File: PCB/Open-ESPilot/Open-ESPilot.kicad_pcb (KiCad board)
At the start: 2 copper layers, 108 parts, among them J1 USB_C_Receptacle_USB2.0_16P, J10 UART1, J11 UART2, J12 I2C, J13 Micro SD Card Breakout, J14 LED out, J2 VOUT, J3 VIN, J4 GND, J5 PWM output, J6 RC in, J7 Vx, J8 GND, J9 UART0, M1 Clone "MP1584" module, M2 GY91, Q1 AO3401A, Q2 BC847, Q3 BC847, SW1 SW_Push, SW2 SW_Push, U1 ESP32-S3-WROOM-1-N8, U2 AMS1117-3.3, U3 AMS1117-3.3, U4 INA219AxD, U5 Micro_SD_Card

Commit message: Started routing. I have few things there. Fixed schematic.
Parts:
- C25, C7, C9, J13, JP12, JP16, JP17, JP25, JP26, JP27, JP28, M1, U3, U5: moved to B.Cu
- C5: footprint Capacitor_THT:CP_Radial_D10.0mm_P5.00mm_P7.50mm -> Capacitor_THT:CP_Radial_D10.0mm_P5.00mm
- TP1, TP2, TP3: footprint TestPoint:TestPoint_THTPad_D2.0mm_Drill1.0mm -> TestPoint:TestPoint_Pad_2.0x2.0mm
- moved U5 310.5 mm to (198.5, -77.0), turned to 90 degrees
- moved J13 309.5 mm to (215.2, -86.8), turned to 180 degrees
- moved JP28 307.9 mm to (198.9, -66.5), turned to 90 degrees
- moved JP27 307.2 mm to (202.5, -66.5), turned to 90 degrees
- moved JP26 306.6 mm to (206.0, -66.5), turned to 90 degrees
- moved C25 304.2 mm to (209.0, -75.3), turned to -90 degrees
- moved J12 230.1 mm to (154.3, -71.2)
- moved R15 225.2 mm to (145.1, -66.1)
- moved R16 225.2 mm to (145.1, -63.2)
- moved C21 217.0 mm to (150.4, -47.2)
- moved JP22 213.7 mm to (133.1, -52.9)
- moved JP23 213.7 mm to (133.1, -49.3)
- moved JP15 192.4 mm to (128.7, -52.9)
- moved JP20 183.4 mm to (133.1, -60.0)
- moved JP21 183.4 mm to (133.1, -56.4)
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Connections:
- C24 pad 2: GND -> Net-(BZ1--)
- J14 pad 1: /Peripheral/5V -> +5V
- J5 pad 1: /Peripheral/ServoOutput1 -> /Peripheral/ServoOutput8
- J5 pad 2: /Peripheral/ServoOutput2 -> /Peripheral/ServoOutput7
- J5 pad 3: /Peripheral/ServoOutput3 -> /Peripheral/ServoOutput6
- J5 pad 4: /Peripheral/ServoOutput4 -> /Peripheral/ServoOutput5
- J5 pad 5: /Peripheral/ServoOutput5 -> /Peripheral/ServoOutput4
- J5 pad 6: /Peripheral/ServoOutput6 -> /Peripheral/ServoOutput3
- J5 pad 7: /Peripheral/ServoOutput7 -> /Peripheral/ServoOutput2
- J5 pad 8: /Peripheral/ServoOutput8 -> /Peripheral/ServoOutput1
- J6 pad 2: /Peripheral/5V -> +5V
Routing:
- net +5V: track 0.00 -> 24.0 mm, vias 0 -> 1
- net GND: track 0.00 -> 17.5 mm, vias 0 -> 1
- net VOUT: track 0.00 -> 16.1 mm
- net /MCU/USB_D+: track 0.00 -> 13.1 mm
- net /MCU/EN: track 0.00 -> 12.9 mm
- net /MCU/USB_D-: track 0.00 -> 12.5 mm
- net +3V3: track 0.00 -> 11.2 mm, vias 0 -> 1
- net /Peripheral/RCin_Inv: track 0.00 -> 11.2 mm, vias 0 -> 2
- net /MCU/GPIO35: track 0.00 -> 10.6 mm
- net Net-(JP2-A): track 0.00 -> 10.1 mm
- net /MCU/GPIO36: track 0.00 -> 9.96 mm
- net /MCU/GPIO44: track 0.00 -> 9.76 mm, vias 0 -> 1
- net Net-(JP3-A): track 0.00 -> 9.19 mm
- net /MCU/GPIO37: track 0.00 -> 9.18 mm
- net /MCU/GPIO38: track 0.00 -> 8.63 mm
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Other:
- board outline added: 50.1 x 91.9 mm

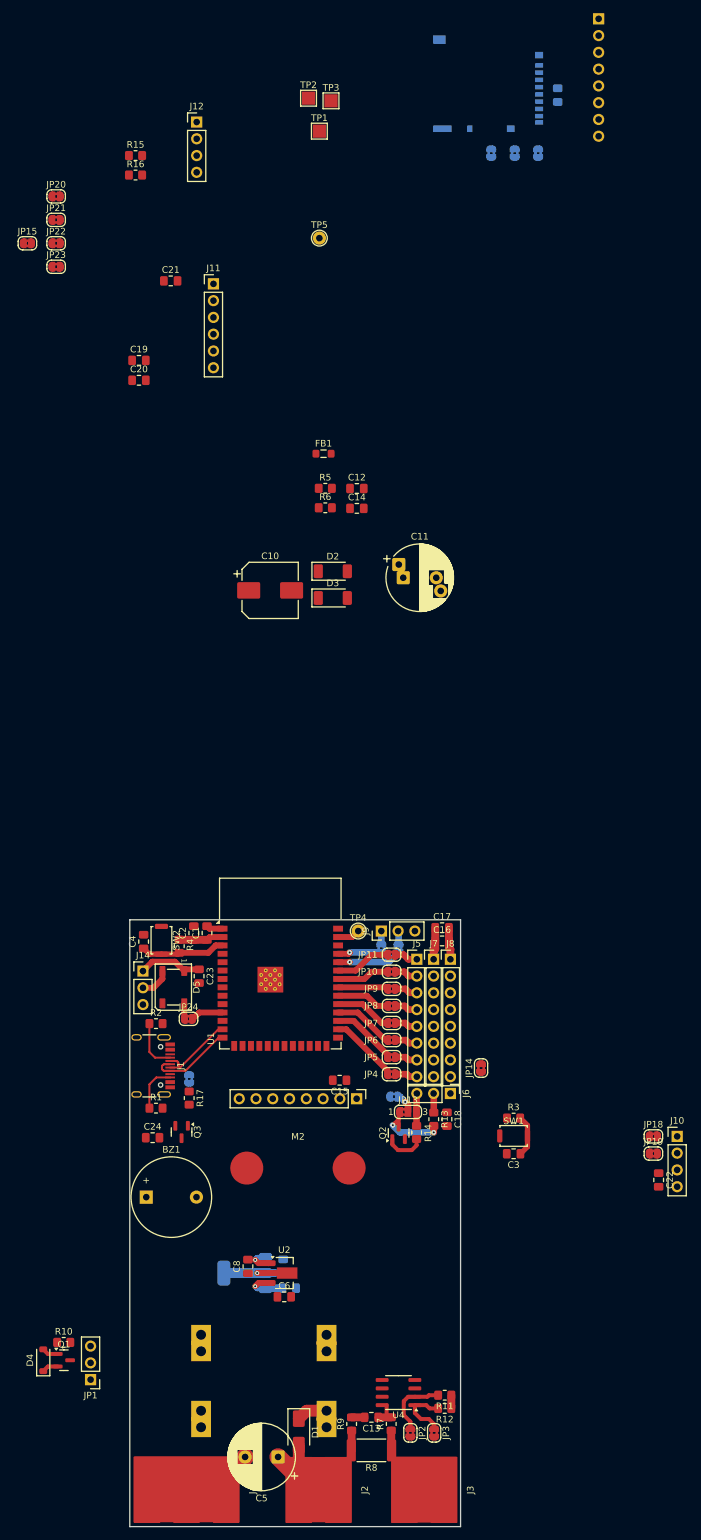
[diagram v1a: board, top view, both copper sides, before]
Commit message: halve of the PCB is routed.
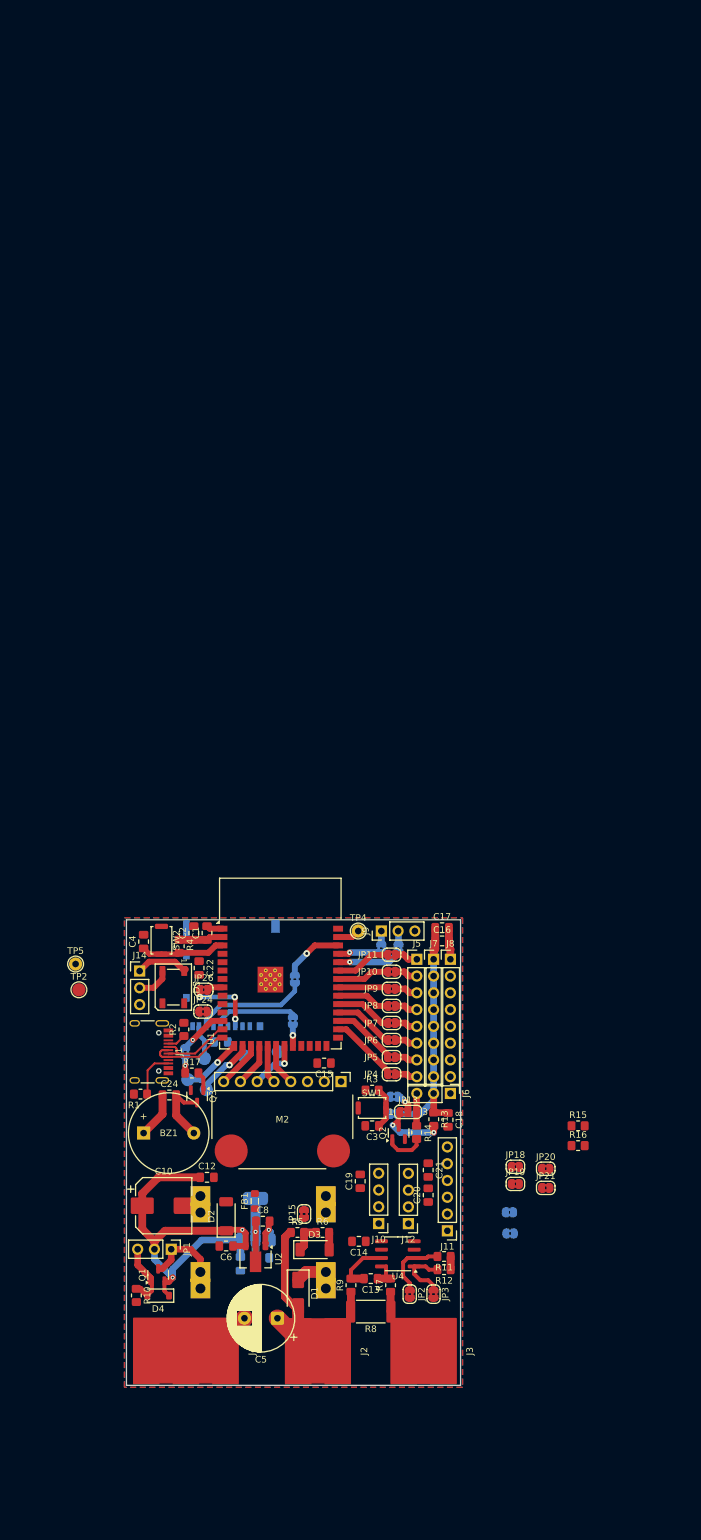
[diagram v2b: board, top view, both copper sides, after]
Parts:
- removed C11: 1000uF, Capacitor_THT:CP_Radial_D10.0mm_P5.00mm_P7.50mm
- removed the C19 at (145.6, -35.1)
- removed J13: Micro SD Card Breakout, Connector_PinHeader_2.54mm:PinHeader_1x08_P2.54mm_Vertical
- added TP6: SD-DAT1, TestPoint:TestPoint_Pad_D2.0mm, B.Cu at (155.5, 70.6)
- added TP7: SD-DAT2, TestPoint:TestPoint_Pad_D2.0mm, B.Cu at (166.7, 69.6)
- added TP8: SD-DAT3, TestPoint:TestPoint_Pad_D2.0mm, B.Cu at (161.5, 70.2)
- JP14: moved to B.Cu
- JP22: renamed from JP23; moved to B.Cu
- JP23: renamed from JP22; moved to B.Cu
- JP26: moved to F.Cu
- M2: footprint GY-90:GY-90 -> GY-91:GY-91
- TP1, TP3: footprint TestPoint:TestPoint_Pad_2.0x2.0mm -> TestPoint:TestPoint_Pad_D2.0mm; moved to B.Cu
- TP2: footprint TestPoint:TestPoint_Pad_2.0x2.0mm -> TestPoint:TestPoint_Pad_D2.0mm
- moved J12 169.9 mm to (186.4, 95.6), turned to 180 degrees
- moved JP23 165.0 mm to (201.8, 97.1), turned to 180 degrees
- moved JP20 164.9 mm to (207.2, 87.3)
- moved JP21 164.3 mm to (207.2, 90.2)
- moved R16 161.5 mm to (212.1, 83.8)
- moved R15 161.5 mm to (212.1, 80.8)
- moved JP22 158.8 mm to (201.7, 93.9), turned to 180 degrees
- moved JP15 152.9 mm to (170.6, 94.2), turned to 90 degrees
- moved C23 152.2 mm to (158.0, 68.1), turned to 180 degrees
- moved TP3 150.9 mm to (155.8, 75.3), turned to 180 degrees
- moved J11 147.7 mm to (192.3, 96.7), turned to 180 degrees
- moved TP1 145.0 mm to (153.0, 73.8), turned to 180 degrees
- moved U5 140.5 mm to (159.6, 58.0), turned to 0 degrees
- moved C21 140.2 mm to (189.4, 87.5), turned to -90 degrees
- moved TP2 139.4 mm to (136.5, 60.2)
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- renumbered C22 to C19, C23 to C22, C25 to C23
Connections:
- C16 pad 1: Net-(J7-Pin_1) -> /Peripheral/+5Vjp
- C17 pad 1: Net-(J7-Pin_1) -> /Peripheral/+5Vjp
- J10 pad 3: /Peripheral/5V -> +5V
- J11 pad 3: /Peripheral/5V -> +5V
- J12 pad 1: /Peripheral/SCL -> /Peripheral/SDA
- J12 pad 2: /Peripheral/SDA -> /Peripheral/SCL
- J12 pad 4: /Peripheral/5V -> +5V
- J6 pad 2: +5V -> /Peripheral/+5Vjp
- J7 pad 1: Net-(J7-Pin_1) -> /Peripheral/+5Vjp
- J7 pad 2: Net-(J7-Pin_1) -> /Peripheral/+5Vjp
- J7 pad 3: Net-(J7-Pin_1) -> /Peripheral/+5Vjp
- J7 pad 4: Net-(J7-Pin_1) -> /Peripheral/+5Vjp
- J7 pad 5: Net-(J7-Pin_1) -> /Peripheral/+5Vjp
- J7 pad 6: Net-(J7-Pin_1) -> /Peripheral/+5Vjp
- J7 pad 7: Net-(J7-Pin_1) -> /Peripheral/+5Vjp
- J7 pad 8: Net-(J7-Pin_1) -> /Peripheral/+5Vjp
- JP14 pad 1: Net-(J7-Pin_1) -> /Peripheral/+5Vjp
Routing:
- net +5V: track 24.0 -> 86.6 mm, vias 1 -> 2
- net /Peripheral/+5Vjp: track 0.00 -> 32.5 mm
- net /Peripheral/SD-DAT0: track 0.00 -> 17.4 mm
- net /Peripheral/SD-CLK: track 0.00 -> 12.9 mm
- net VOUT: track 16.1 -> 28.9 mm
- net /Power/+5Vreg: track 0.00 -> 10.9 mm
- net /Peripheral/SD-CMD: track 0.00 -> 10.9 mm, vias 0 -> 3
- net Net-(BZ1--): track 0.00 -> 10.5 mm
- net /MCU/GPIO2: track 0.00 -> 9.25 mm, vias 0 -> 1
- net /MCU/GPIO46: track 0.00 -> 9.16 mm, vias 0 -> 1
- net /MCU/GPIO3: track 0.00 -> 9.13 mm, vias 0 -> 1
- net /MCU/GPIO13: track 0.00 -> 7.98 mm, vias 0 -> 1
- net /Power/+5Vusb: track 2.48 -> 10.4 mm
- net /MCU/GPIO8: track 0.00 -> 7.32 mm, vias 0 -> 1
- net /MCU/GPIO9: track 0.00 -> 7.11 mm
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- added copper zone on B.Cu, net GND
- added copper zone on F.Cu, net GND
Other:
- board size 50.1 x 91.9 mm -> 50.6 x 70.5 mm

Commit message: I'm rushing it! :( Finished the PCB
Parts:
- C15, JP18, JP19, JP20, JP21, TP2: moved to B.Cu
- JP12: moved to F.Cu
- TP5: footprint TestPoint:TestPoint_THTPad_D2.0mm_Drill1.0mm -> TestPoint:TestPoint_Pad_D2.0mm; moved to B.Cu
- moved R15 36.0 mm to (178.1, 92.6)
- moved TP2 35.7 mm to (171.8, 65.8), turned to 180 degrees
- moved R16 35.7 mm to (178.1, 94.6)
- moved TP5 34.2 mm to (170.0, 52.9), turned to 180 degrees
- moved JP23 27.6 mm to (177.3, 84.4), turned to 90 degrees
- moved JP22 23.5 mm to (179.0, 87.8), turned to 90 degrees
- moved R10 19.5 mm to (164.3, 102.7), turned to 90 degrees
- moved JP19 18.2 mm to (184.4, 89.6), turned to 90 degrees
- moved JP20 17.6 mm to (189.8, 85.0), turned to 90 degrees
- moved JP21 17.2 mm to (192.3, 81.6), turned to 90 degrees
- moved JP18 14.9 mm to (188.8, 92.5), turned to 90 degrees
- moved D4 13.4 mm to (161.7, 104.0), turned to -90 degrees
- moved C19 10.4 mm to (189.4, 87.5)
- moved C21 10.4 mm to (179.0, 87.2)
- moved Q1 10.1 mm to (158.6, 104.0), turned to 180 degrees
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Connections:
- J6 pad 2: /Peripheral/+5Vjp -> +5V
- R3 pad 1: /MCU/+3V3p -> +3V3
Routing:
- net +5V: track 86.6 -> 235.2 mm, vias 2 -> 1
- net +3V3: track 12.8 -> 79.5 mm, vias 1 -> 3
- net /MCU/+3V3p: track 6.74 -> 68.3 mm, vias 0 -> 4
- net GND: track 21.4 -> 79.9 mm, vias 1 -> 57
- net /MCU/GPIO4: track 0.00 -> 55.9 mm, vias 0 -> 2
- net /Power/+5Vusb: track 10.4 -> 65.8 mm, vias 0 -> 2
- net /MCU/GPIO6: track 0.00 -> 55.2 mm, vias 0 -> 1
- net /MCU/GPIO16: track 0.00 -> 50.4 mm, vias 0 -> 1
- net /MCU/GPIO7: track 0.00 -> 49.0 mm, vias 0 -> 1
- net /MCU/GPIO17: track 0.00 -> 48.5 mm, vias 0 -> 1
- net /Peripheral/SCL: track 0.00 -> 33.1 mm, vias 0 -> 1
- net /Peripheral/SDA: track 0.00 -> 29.6 mm
- net /MCU/GPIO48: track 0.00 -> 24.5 mm, vias 0 -> 1
- net /MCU/GPIO47: track 0.00 -> 20.1 mm, vias 0 -> 1
- net /MCU/GPIO21: track 0.00 -> 18.6 mm
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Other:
- board size 50.6 x 70.5 mm -> 50.6 x 71.1 mm

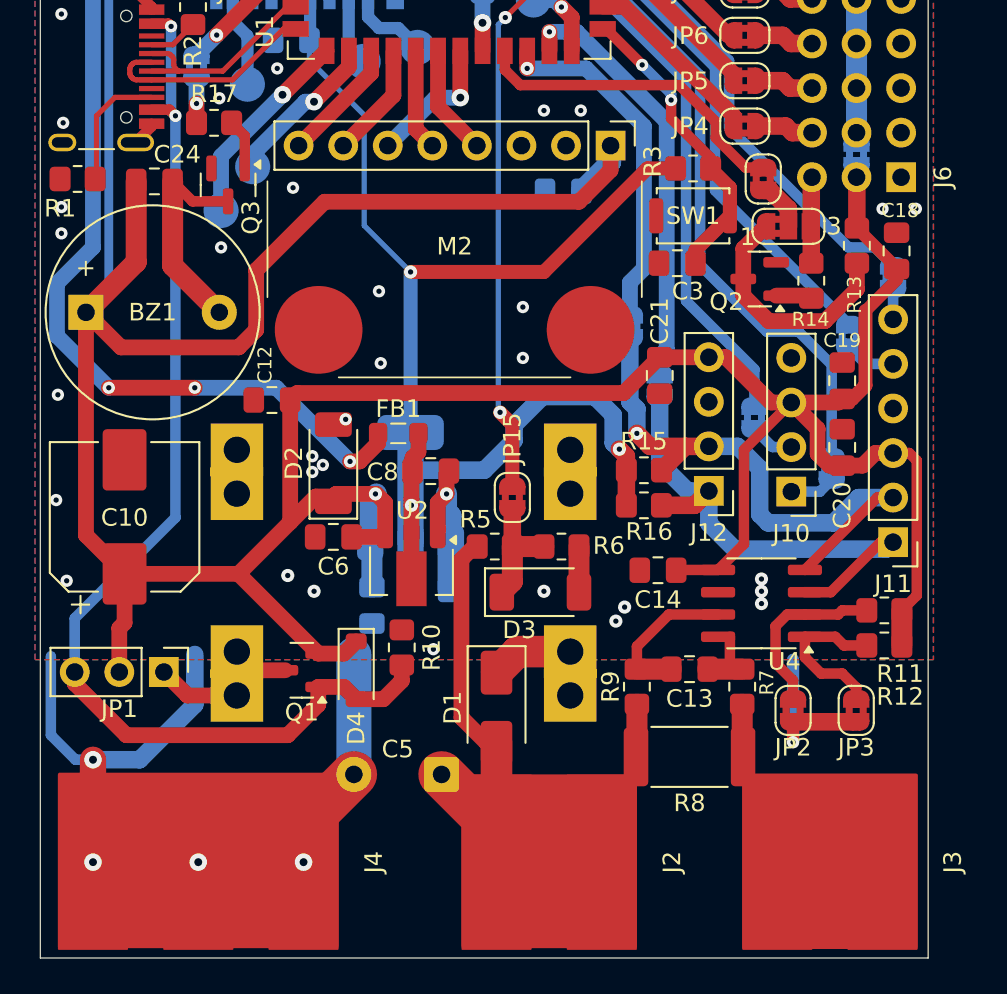
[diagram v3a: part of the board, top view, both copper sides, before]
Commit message: Added labels to headers.
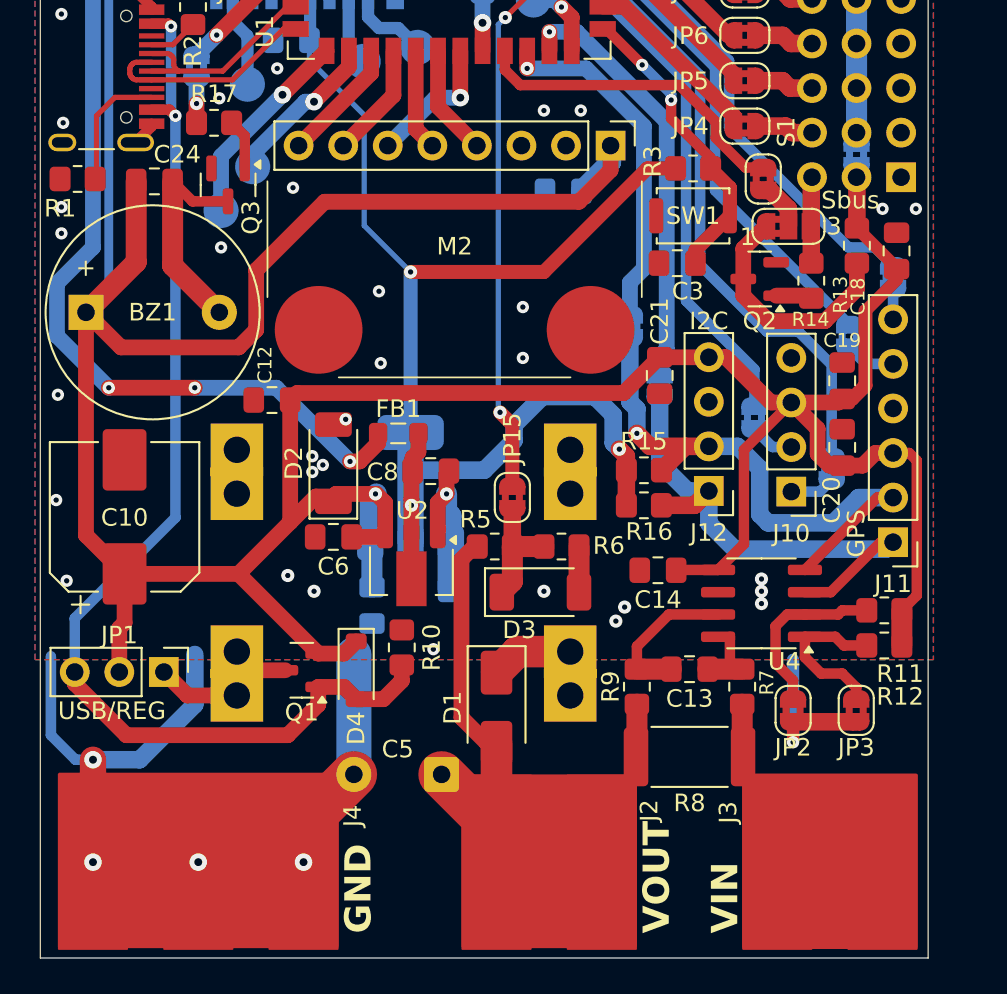
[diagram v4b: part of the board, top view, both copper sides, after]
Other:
- board text added: "GND"
- board text added: "GPS"
- board text added: "I2C"
- board text added: "S1"
- board text added: "Sbus"
- board text added: "USB/REG"
- board text added: "VIN"
- board text added: "VOUT"
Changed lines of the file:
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@@
 		(at 158.7 114.9375 90)
 		(property "Reference" "J4"
-			(at 0 4 90)
+			(at 2.6375 2.8 90)
 			(unlocked yes)
 			(layer "F.SilkS")
@@
 		(tags "capacitor handsolder")
 		(property "Reference" "C18"
-			(at 2.3 0.2 180)
+			(at -2.6 -2.2 270)
 			(layer "F.SilkS")
 			(effects
@@
 		(at 175.7 114.9375 90)
 		(property "Reference" "J2"
-			(at 0 4 90)
+			(at 2.9375 2.7 90)
 			(unlocked yes)
 			(layer "F.SilkS")
@@
 		(tags "SOT TO_SOT_SMD")
 		(property "Reference" "Q2"
-			(at 1.9 -1.3 0)
+			(at 0 -2.4 0)
 			(layer "F.SilkS")
 			(effects
@@
 		(tags "Through hole pin header THT 1x03 2.54mm single row")
 		(property "Reference" "JP1"
-			(at 2.1 2.54 180)
+			(at -2.1 2.54 180)
 			(layer "F.SilkS")
 			(effects
@@
 		(at 191.7 114.9375 90)
 		(property "Reference" "J3"
-			(at 0 4 90)
+			(at 2.8375 -8.8 90)
 			(unlocked yes)
 			(layer "F.SilkS")
@@
 			(at 0 -2.38 90)
 			(layer "F.SilkS")
+			(hide yes)
 			(effects
 				(font
@@
 		(tags "resistor handsolder")
 		(property "Reference" "R13"
-			(at 2.8 0.1375 270)
+			(at 2.8 0.9375 270)
 			(layer "F.SilkS")
 			(effects
@@
 		(tags "capacitor handsolder")
 		(property "Reference" "C20"
-			(at -3.3 0 90)
+			(at -3 -0.6 90)
 			(layer "F.SilkS")
 			(effects
@@
 		(layer "Edge.Cuts")
 	)
+	(gr_text "VIN"
+		(at 183.6 119 90)
+		(layer "F.SilkS")
+		(effects
+			(font
+				(size 1.5 1.5)
+				(thickness 0.3)
+				(bold yes)
+			)
+			(justify left bottom)
+		)
+	)
+	(gr_text "GND"
+		(at 162.7 119 90)
+		(layer "F.SilkS")
+		(effects
+			(font
+				(size 1.5 1.5)
+				(thickness 0.3)
+				(bold yes)
+			)
+			(justify left bottom)
+		)
+	)
+	(gr_text "S1"
+		(at 186.8 74.2 90)
+		(layer "F.SilkS")
+		(effects
+			(font
+				(size 1 1)
+				(thickness 0.1)
+			)
+			(justify left bottom)
+		)
+	)
+	(gr_text "USB/REG"
+		(at 144.7 106.9 0)
+		(layer "F.SilkS")
+		(effects
+			(font
+				(size 1 1)
+				(thickness 0.1)
+			)
+			(justify left bottom)
+		)
+	)
+	(gr_text "GPS"
+		(at 190.2 96.2 90)
+		(layer "F.SilkS")
+		(effects
+			(font
+				(size 1 1)
+				(thickness 0.1)
+			)
+		)
+	)
+	(gr_text "Sbus"
+		(at 188.2 77.8 0)
+		(layer "F.SilkS")
+		(effects
+			(font
+				(size 1 1)
+				(thickness 0.1)
+			)
+			(justify left bottom)
+		)
+	)
+	(gr_text "I2C"
+		(at 181.8 84.1 0)
+		(layer "F.SilkS")
+		(effects
+			(font
+				(size 1 1)
+				(thickness 0.1)
+			)
+		)
+	)
+	(gr_text "VOUT"
+		(at 179.7 119 90)
+		(layer "F.SilkS")
+		(effects
+			(font
+				(size 1.5 1.5)
+				(thickness 0.3)
+				(bold yes)
+			)
+			(justify left bottom)
+		)
+	)
 	(segment

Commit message: Preparing to order
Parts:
- moved JP22 35.1 mm to (151.3, 109.3)
- moved JP19 32.8 mm to (151.9, 93.8)
- moved JP18 31.7 mm to (157.1, 94.2)
- moved JP23 31.4 mm to (147.4, 94.0)
- moved J11 29.7 mm to (164.7, 107.7)
- moved J12 29.7 mm to (154.2, 104.8)
- moved J5 29.7 mm to (160.1, 66.6)
- moved J9 29.7 mm to (154.7, 62.3)
- moved JP16 29.7 mm to (154.7, 64.9)
- moved JP21 29.7 mm to (164.7, 92.6)
- moved JP28 29.7 mm to (141.7, 72.9)
- moved R10 29.7 mm to (136.7, 113.7)
- moved R11 29.7 mm to (164.2, 111.6)
- moved R12 29.7 mm to (164.2, 113.6)
- moved R13 29.7 mm to (162.6, 90.8)
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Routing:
- net /MCU/GPIO6: track 55.2 -> 42.9 mm
- net /MCU/GPIO48: track 24.5 -> 35.8 mm
- net /Peripheral/U1-TX: track 2.58 -> 13.7 mm
- net /MCU/GPIO7: track 49.0 -> 39.3 mm
- net /Peripheral/U1-RX: track 2.53 -> 11.9 mm
- net /Peripheral/SCL: track 33.1 -> 36.1 mm
- net /MCU/GPIO16: track 50.4 -> 47.5 mm
- net /Peripheral/U2-TX: track 2.89 -> 5.64 mm
- net /Peripheral/SDA: track 29.6 -> 28.1 mm
- net /MCU/GPIO4: track 55.9 -> 56.7 mm
- net /MCU/GPIO47: track 20.1 -> 19.5 mm
- net /MCU/GPIO0: track 17.3 -> 17.9 mm
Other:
- board text added: "5V"
- board text added: "5V switching regulator Clone {dblquote}MP1584{dblquote} module"
- board text added: "Alternative LDO AMS1117-3.3"
- board text added: "Created by Tomáš Kuchta couldn't have done it without this awesome community!"
- board text added: "ELRS"
- board text added: "ESP32-S3"
- board text added: "GND 5V SBUS"
- board text added: "GPIO1"
- board text added: "GY91"
- board text added: "Micro SD Card"
- board text added: "Open ESPilot"
- board text added: "Open-ESPilot"
- board text added: "S2"
- board text added: "S3"
- board text added: "S4"
- board text added: "S5"
- board text added: "S6"
- board text added: "S7"
- board text added: "SDA SCL 5V GND TX RX"
- board text added: "SDA SCL GND 5V"
- board text added: "SHUNT"
- board text added: "Sx"
- board text added: "TX RX 5V GND"
- board text added: "Tk"
- board text added: "USB-C!"
- board text added: "VERSION 1"
- board text added: "WS2811 5V DOUT GND"
